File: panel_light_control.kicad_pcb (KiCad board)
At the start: 2 copper layers, 103 parts, among them J1 Conn_01x02, J10 Conn_01x09, J11 RJ45_Shielded, J12 RJ45_Shielded, J13 HR911105A, J2 Conn_01x02, J3 Conn_01x02, J4 Conn_01x04, J5 Conn_01x06, J6 Conn_01x04, J7 Conn_01x04, J8 Conn_01x07, J9 Conn_01x06, Q1 IRF540N, Q2 IRF540N, Q3 IRF540N, U1 L7805, U2 LM324, U3 STM32F207VGTx, U4 MCP2562-E-P, U5 LAN8720A, Y1 Crystal_GND24

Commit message: Started layouting.
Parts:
- added D3: D_Small, Diode_SMD:D_0603_1608Metric, F.Cu at (70.2, 67.2)
- added F1: Polyfuse_Small, Fuse:Fuse_1206_3216Metric, F.Cu at (70.7, 72.3)
- C13, C14: value 100nF -> 4.7uF
- moved C2 80.8 mm to (74.0, 67.1), turned to 90 degrees
- moved C3 75.1 mm to (77.2, 67.0), turned to 90 degrees
- moved D2 67.7 mm to (87.4, 78.2)
- moved D1 65.1 mm to (86.8, 71.4)
- moved C7 58.8 mm to (88.7, 84.7), turned to 180 degrees
- moved C13 55.9 mm to (189.2, 109.2), turned to 180 degrees
- moved C29 50.7 mm to (140.9, 104.0)
- moved C12 42.4 mm to (105.2, 70.7), turned to 90 degrees
- moved R31 37.3 mm to (133.0, 102.5)
- moved R5 32.0 mm to (140.7, 60.8)
- moved R32 30.4 mm to (125.8, 110.6)
- moved C32 30.4 mm to (121.3, 103.0)
- moved R6 28.2 mm to (131.9, 69.5)
- moved C5 27.4 mm to (125.0, 72.0)
- moved R8 22.0 mm to (139.7, 67.3)
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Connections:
- J1 pad 2: +24V -> Net-(F1-Pad2)

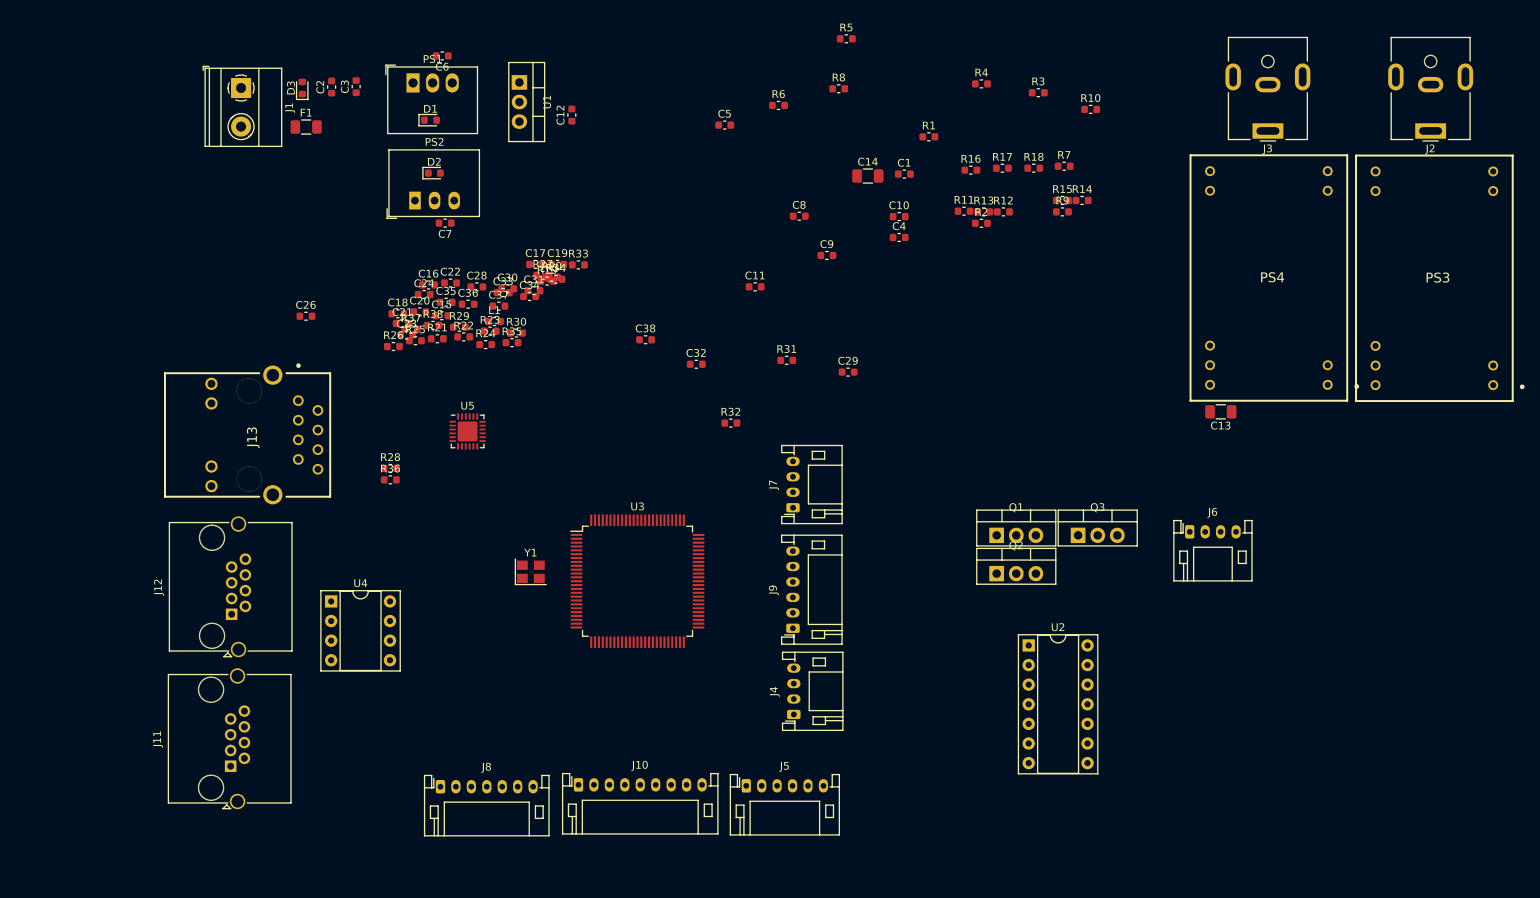
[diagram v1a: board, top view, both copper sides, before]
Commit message: Sorted passives on board.
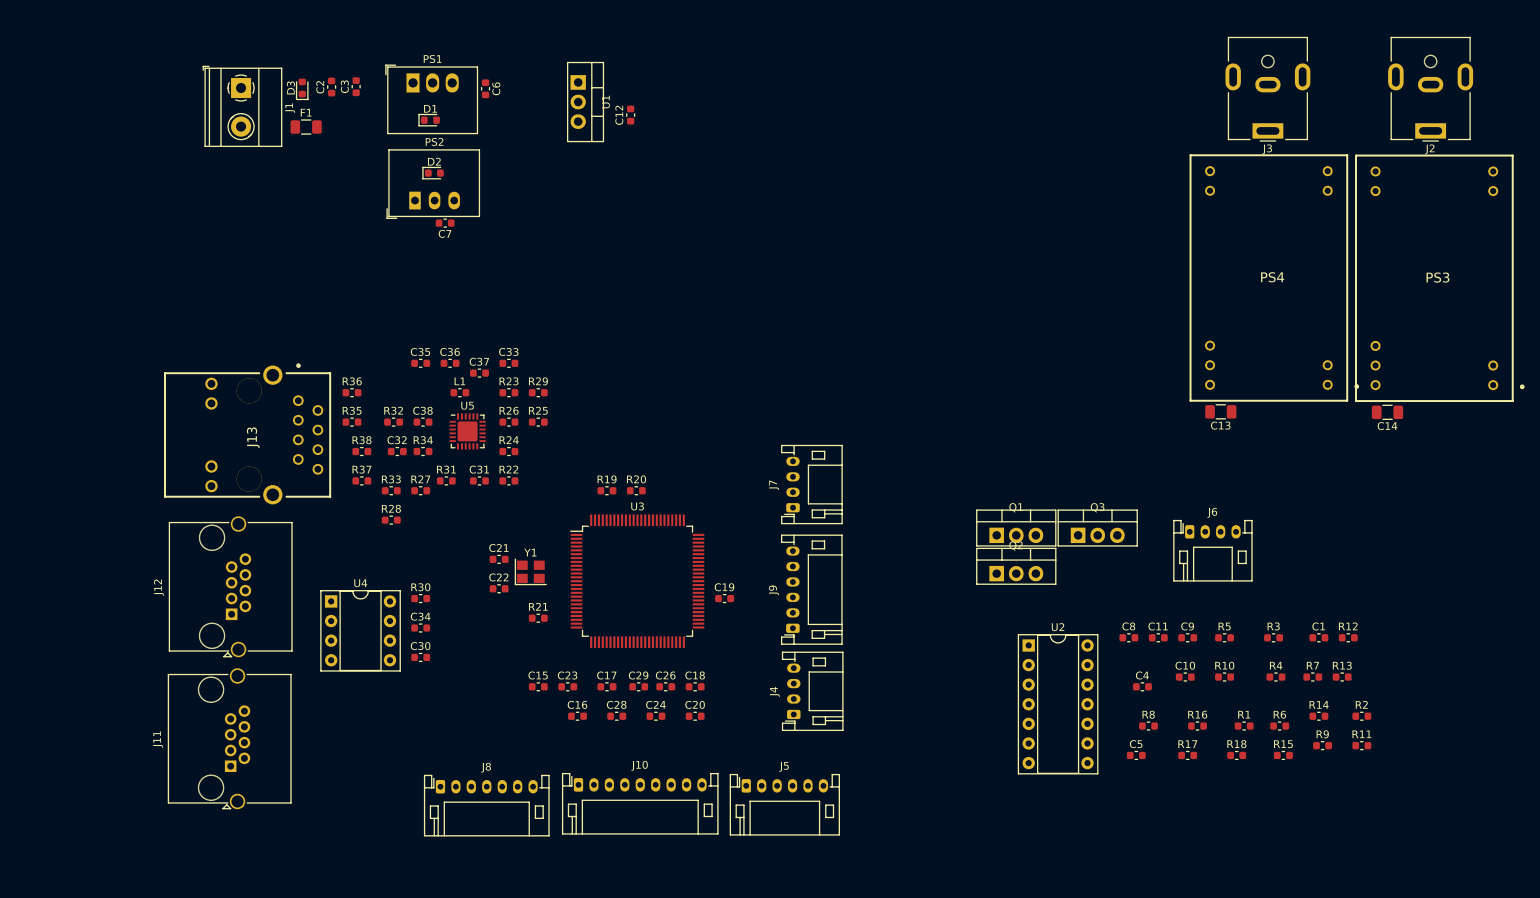
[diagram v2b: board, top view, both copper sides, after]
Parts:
- moved R6 103.3 mm to (196.8, 149.9)
- moved C5 97.5 mm to (178.3, 153.7)
- moved R8 91.8 mm to (179.9, 149.9)
- moved R5 91.8 mm to (189.7, 138.4)
- moved R1 86.6 mm to (192.3, 149.9)
- moved R11 86.3 mm to (207.5, 152.4)
- moved R4 85.8 mm to (196.4, 143.5)
- moved R2 80.7 mm to (207.5, 148.6)
- moved C1 80.6 mm to (201.9, 138.4)
- moved R18 80.5 mm to (191.3, 153.7)
- moved R17 79.8 mm to (184.9, 153.7)
- moved R16 77.8 mm to (186.2, 149.9)
- moved R15 77.4 mm to (197.3, 153.7)
- moved R9 76.9 mm to (202.4, 152.4)
- moved R3 76.9 mm to (196.1, 138.4)
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
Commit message: Finished initial layout LED CV, CAN.
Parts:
- added H1: MountingHole, MountingHole:MountingHole_3.2mm_M3_DIN965, F.Cu at (77.0, 160.6)
- added H2: MountingHole, MountingHole:MountingHole_3.2mm_M3_DIN965, F.Cu at (179.2, 69.5)
- added H3: MountingHole, MountingHole:MountingHole_3.2mm_M3_DIN965, F.Cu at (57.4, 92.4)
- added H4: MountingHole, MountingHole:MountingHole_3.2mm_M3_DIN965, F.Cu at (173.9, 148.6)
- moved R2 71.1 mm to (136.7, 142.5)
- moved R9 67.9 mm to (141.7, 121.9)
- moved C1 65.6 mm to (136.7, 145.3), turned to 180 degrees
- moved R11 64.0 mm to (144.3, 142.0), turned to 270 degrees
- moved R12 62.3 mm to (144.3, 127.8), turned to 90 degrees
- moved R3 62.0 mm to (134.2, 142.0), turned to 270 degrees
- moved R7 59.9 mm to (141.4, 148.2), turned to 180 degrees
- moved R1 55.6 mm to (136.6, 148.3), turned to 180 degrees
- moved R14 52.0 mm to (152.5, 132.4), turned to 180 degrees
- moved C13 51.1 mm to (138.2, 112.0)
- moved C14 51.1 mm to (159.8, 112.0)
- moved J3 51.1 mm to (144.3, 75.6)
- moved PS3 51.1 mm to (165.8, 94.7)
- moved PS4 51.1 mm to (144.4, 94.6)
- moved J2 51.1 mm to (165.4, 75.6)
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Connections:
- C5 pad 2: +3.3V -> +5V
- U2 pad 4: +3.3V -> +5V

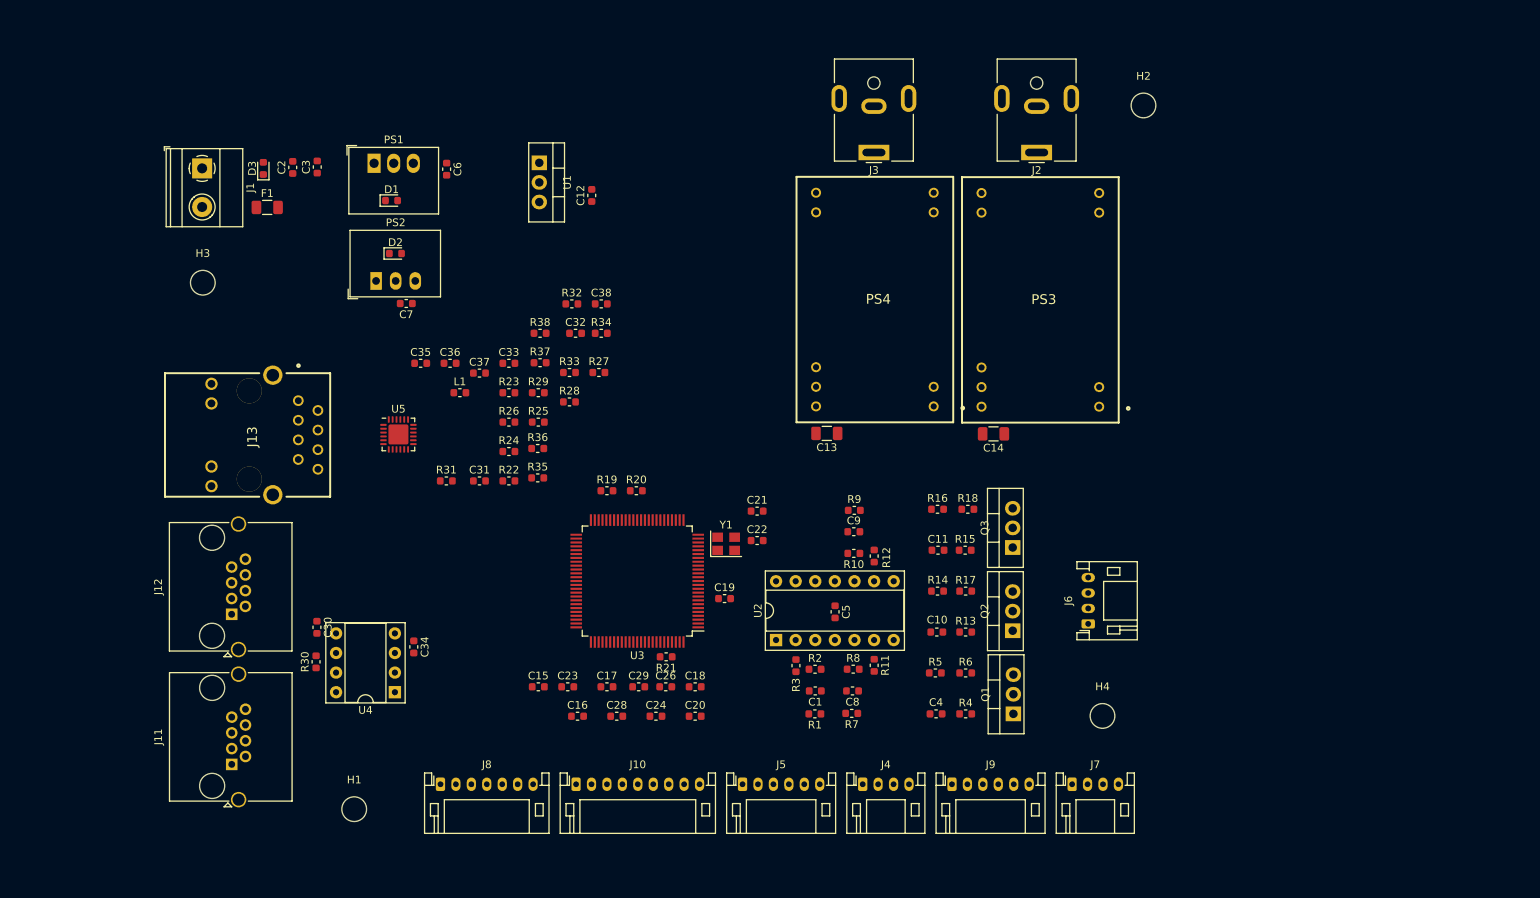
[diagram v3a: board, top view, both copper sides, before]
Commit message: Finished basic board layout.
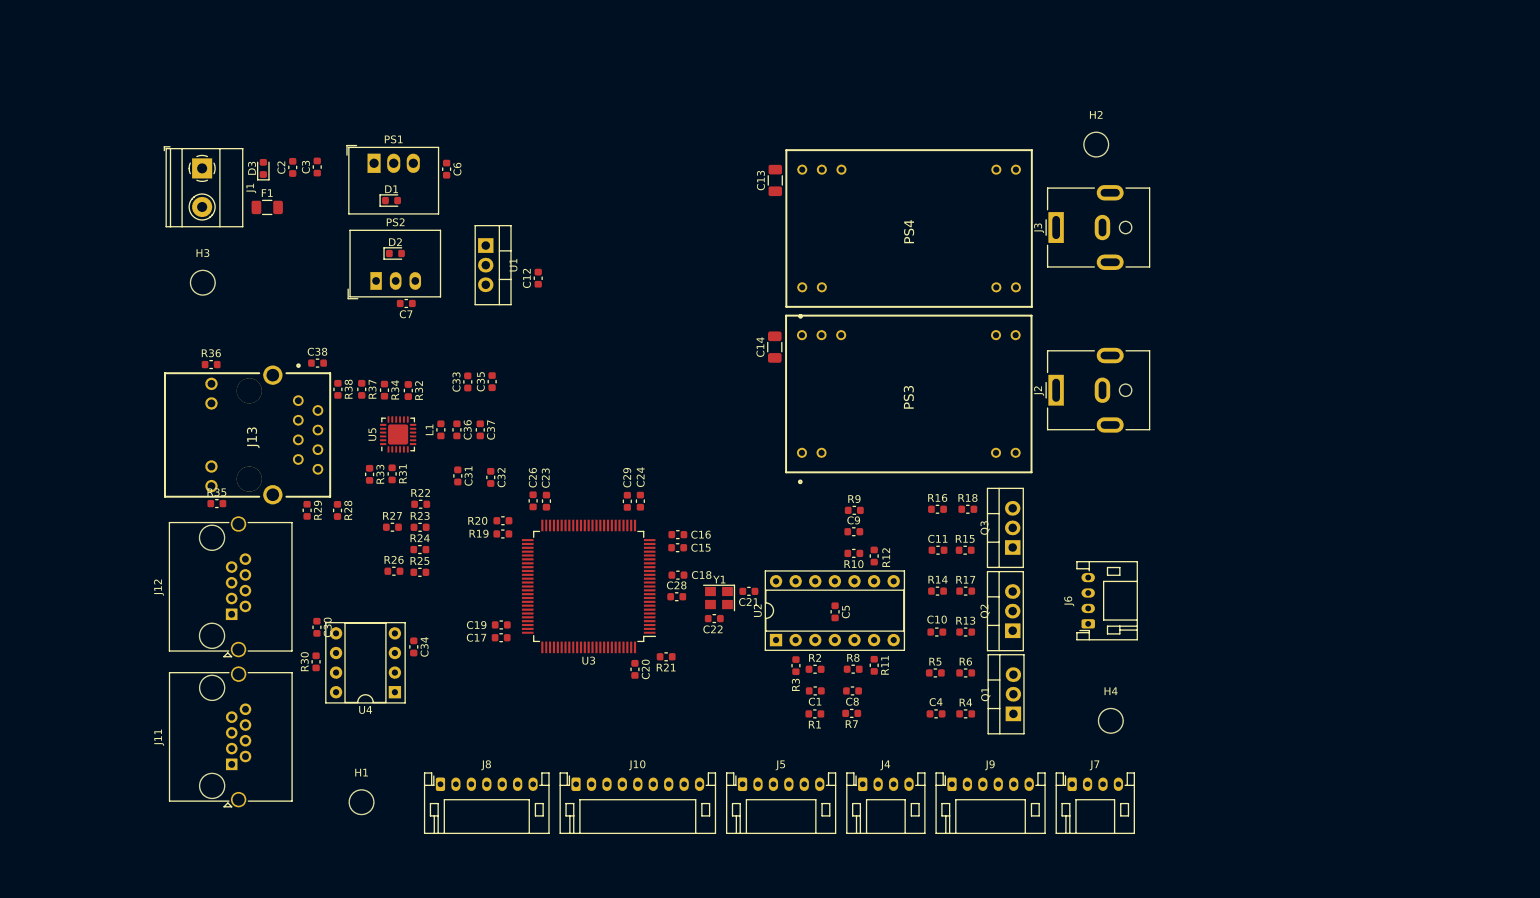
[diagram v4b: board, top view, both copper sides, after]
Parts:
- R32, R34, R37, R38: value 50 -> 49.9
- moved R36 43.7 mm to (58.4, 103.0)
- moved R35 41.7 mm to (59.2, 121.0)
- moved C38 37.5 mm to (72.2, 102.8)
- moved R29 33.6 mm to (70.9, 121.9), turned to 270 degrees
- moved C13 33.4 mm to (131.5, 79.2), turned to 90 degrees
- moved R27 33.4 mm to (81.9, 124.1)
- moved R28 33.2 mm to (74.8, 121.9), turned to 270 degrees
- moved J2 30.9 mm to (167.9, 106.4), turned to 90 degrees
- moved C14 30.5 mm to (131.4, 100.8), turned to 90 degrees
- moved C26 29.6 mm to (100.1, 120.7), turned to 90 degrees
- moved C19 29.1 mm to (96.0, 136.8), turned to 180 degrees
- moved R33 29.1 mm to (79.0, 117.3), turned to 270 degrees
- moved R34 29.0 mm to (80.9, 106.3), turned to 270 degrees
- moved C24 27.9 mm to (114.0, 120.7), turned to 90 degrees
- moved R38 27.2 mm to (74.9, 106.2), turned to 270 degrees
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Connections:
- J13 pad 2: VDDA -> Net-(J13-Pad2)
- R34 pad 2: VDDA -> Net-(J13-Pad2)
- U5 pad 20: VDDA -> Net-(J13-Pad2)
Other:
- copper layers 2 -> 4

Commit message: Board layout tweaks.
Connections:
- C5 pad 2: +5V -> +12V
- U2 pad 4: +5V -> +12V
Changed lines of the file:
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@@
       (net 2 GND))
     (pad 2 smd roundrect (at 0.7875 0 270) (size 0.875 0.95) (layers F.Cu F.Paste F.Mask) (roundrect_rratio 0.25)
-      (net 14 +5V))
+      (net 7 +12V))
     (model ${KISYS3DMOD}/Capacitor_SMD.3dshapes/C_0603_1608Metric.wrl
       (at (xyz 0 0 0))
@@
       (net 9 "Net-(C9-Pad2)"))
     (pad 4 thru_hole oval (at 0 7.62 90) (size 1.6 1.6) (drill 0.8) (layers *.Cu *.Mask)
-      (net 14 +5V))
+      (net 7 +12V))
     (pad 11 thru_hole oval (at 7.62 7.62 90) (size 1.6 1.6) (drill 0.8) (layers *.Cu *.Mask)
       (net 2 GND))

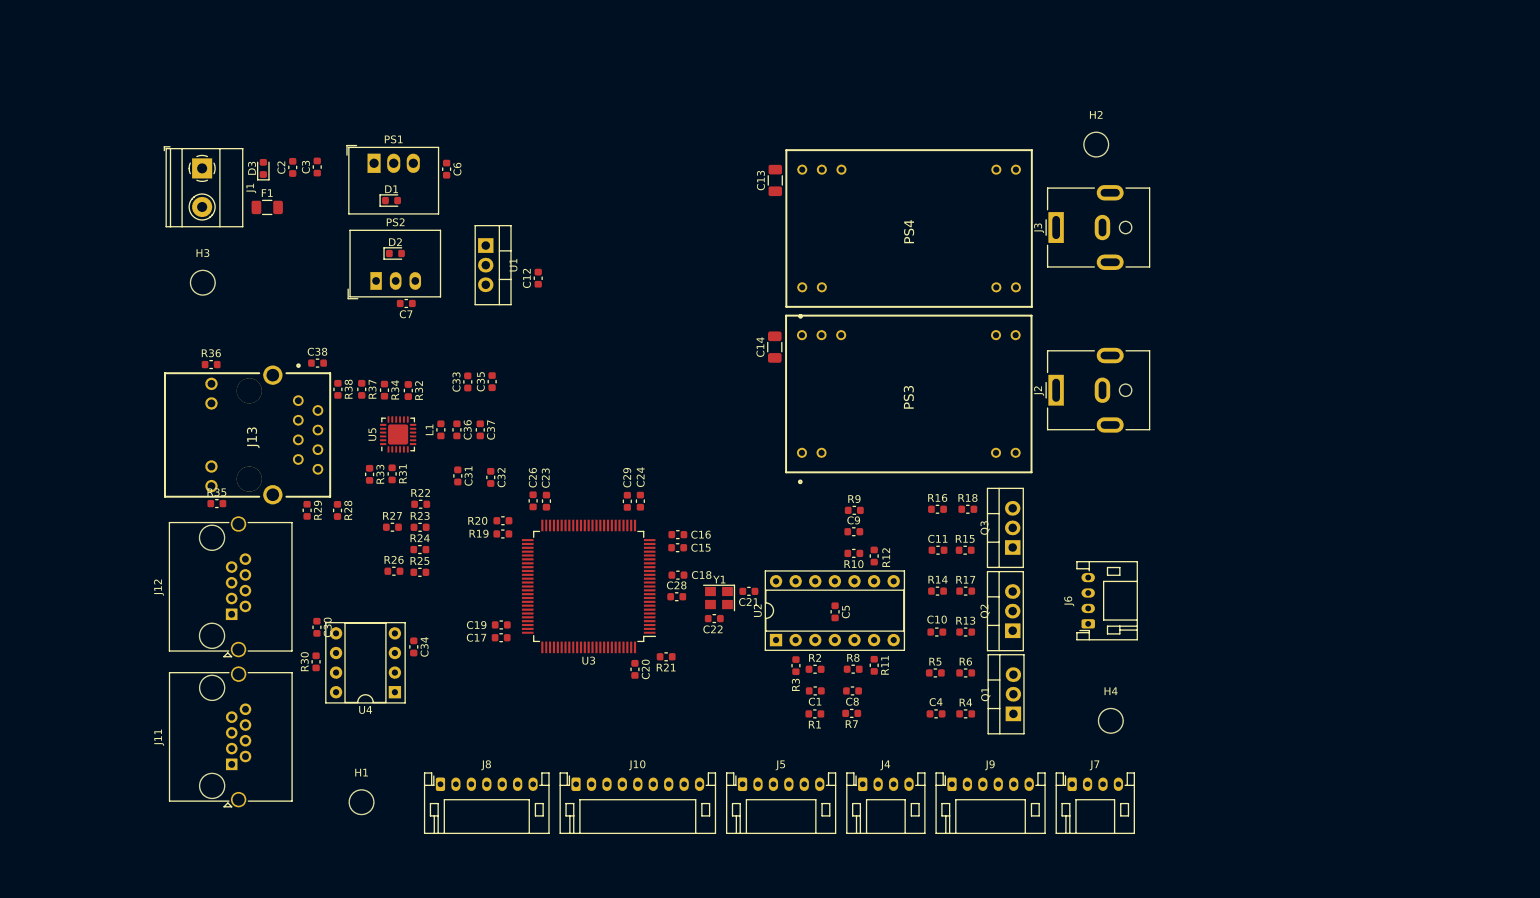
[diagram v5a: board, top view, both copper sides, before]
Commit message: Tweaking power section layout.
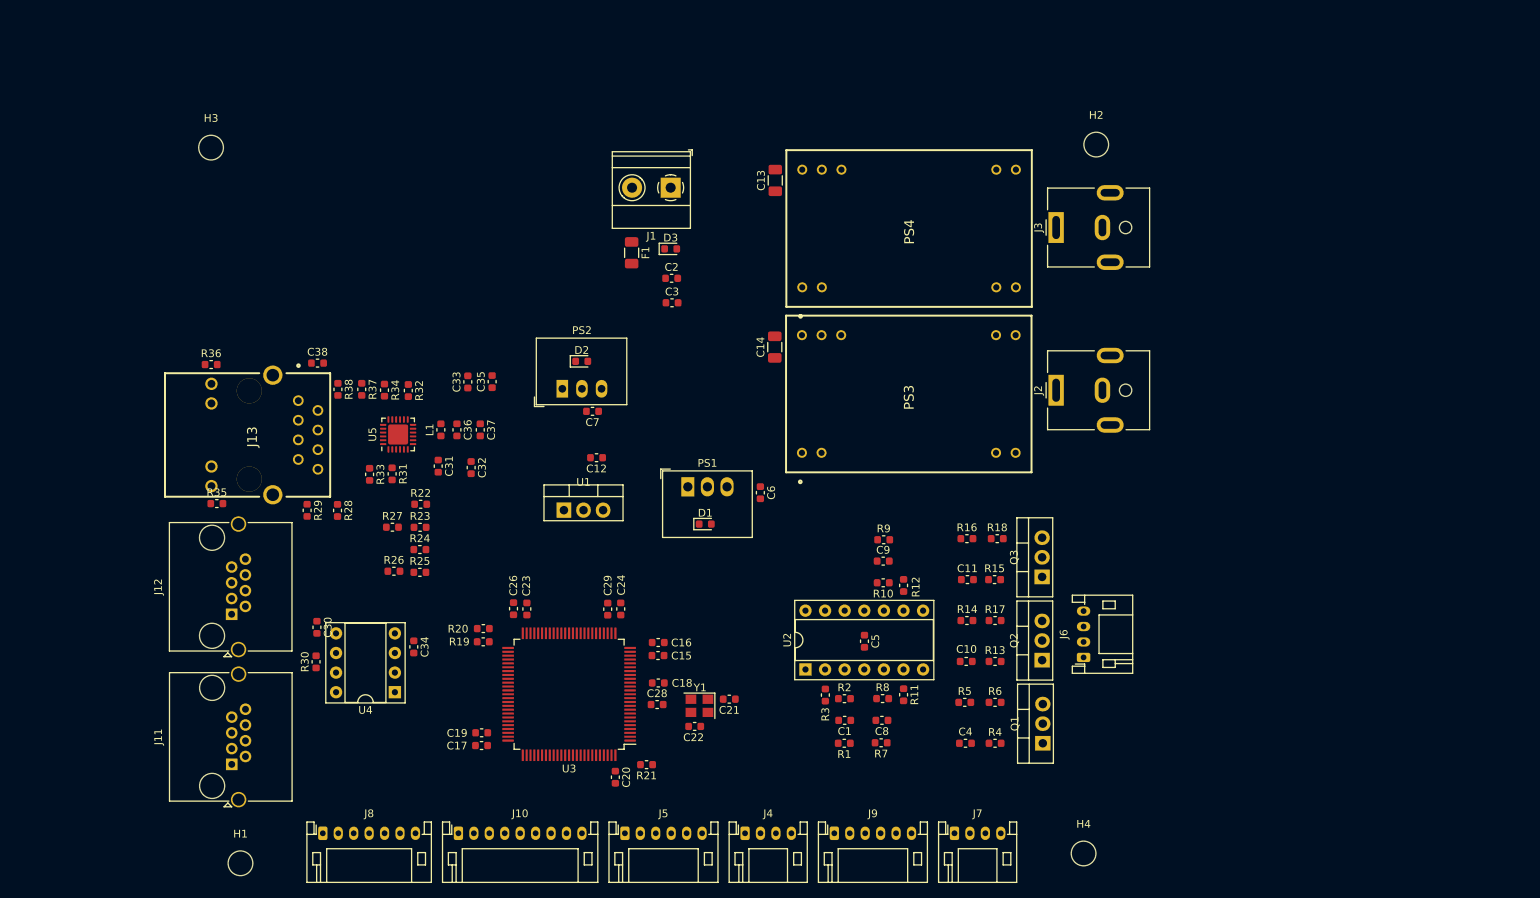
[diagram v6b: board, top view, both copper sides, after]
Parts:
- moved J1 60.7 mm to (118.0, 80.1), turned to 180 degrees
- moved C6 58.4 mm to (129.6, 119.6)
- moved D1 58.4 mm to (122.4, 123.7)
- moved PS1 58.4 mm to (120.2, 118.9)
- moved D3 53.8 mm to (118.0, 88.0), turned to 0 degrees
- moved C2 51.1 mm to (118.1, 91.9), turned to 0 degrees
- moved C3 49.2 mm to (118.1, 95.0), turned to 0 degrees
- moved F1 47.6 mm to (112.9, 88.6), turned to 270 degrees
- moved U1 35.7 mm to (104.1, 121.9), turned to 0 degrees
- moved C7 27.9 mm to (107.8, 109.1)
- moved D2 27.9 mm to (106.4, 102.6)
- moved PS2 27.9 mm to (103.9, 106.2)
- moved C12 24.5 mm to (108.4, 115.1), turned to 180 degrees
- moved H1 17.6 mm to (62.2, 167.6)
- moved H4 17.5 mm to (171.4, 166.4)
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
